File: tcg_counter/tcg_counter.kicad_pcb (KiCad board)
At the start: 2 copper layers, 63 x 88 mm, 21 parts, among them P1 TC2050-IDC-430, U1 TCAL9539RTW, U3 RF430FRL152

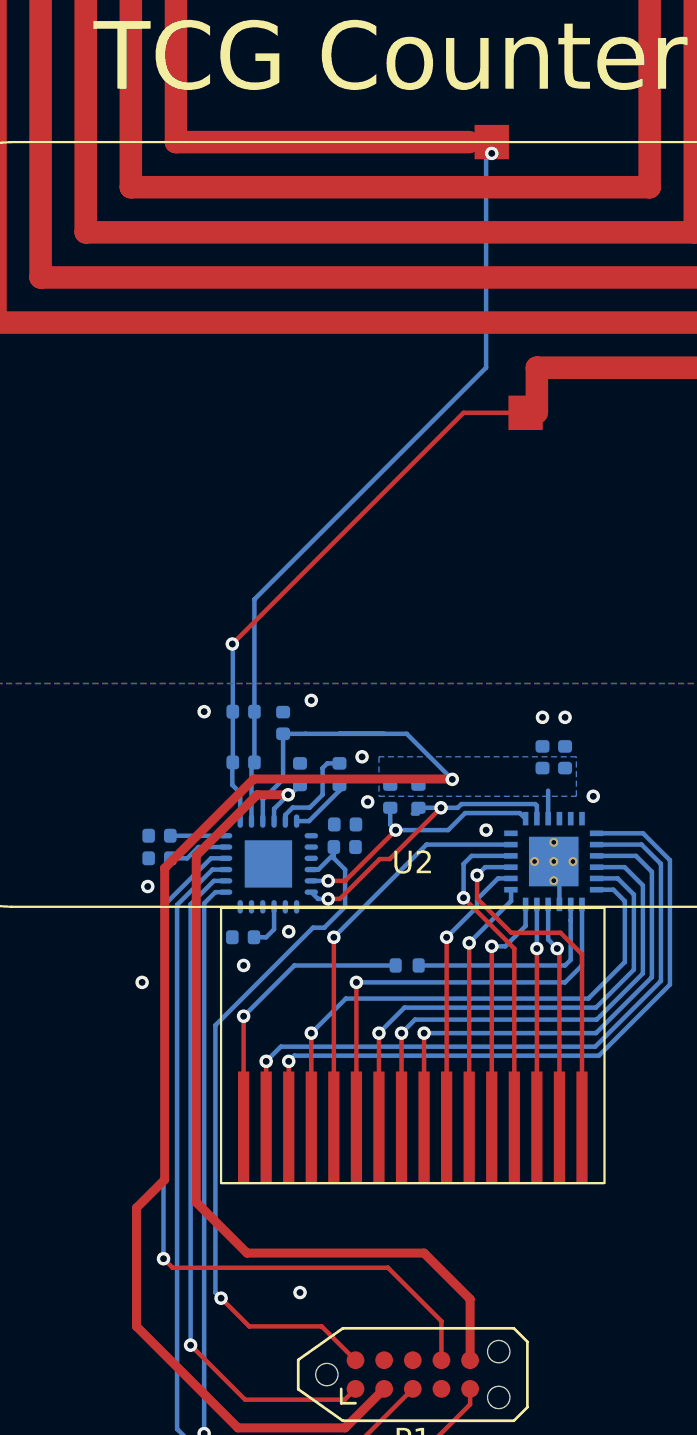
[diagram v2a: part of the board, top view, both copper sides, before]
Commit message: Cleaned up pad vias and solder paste
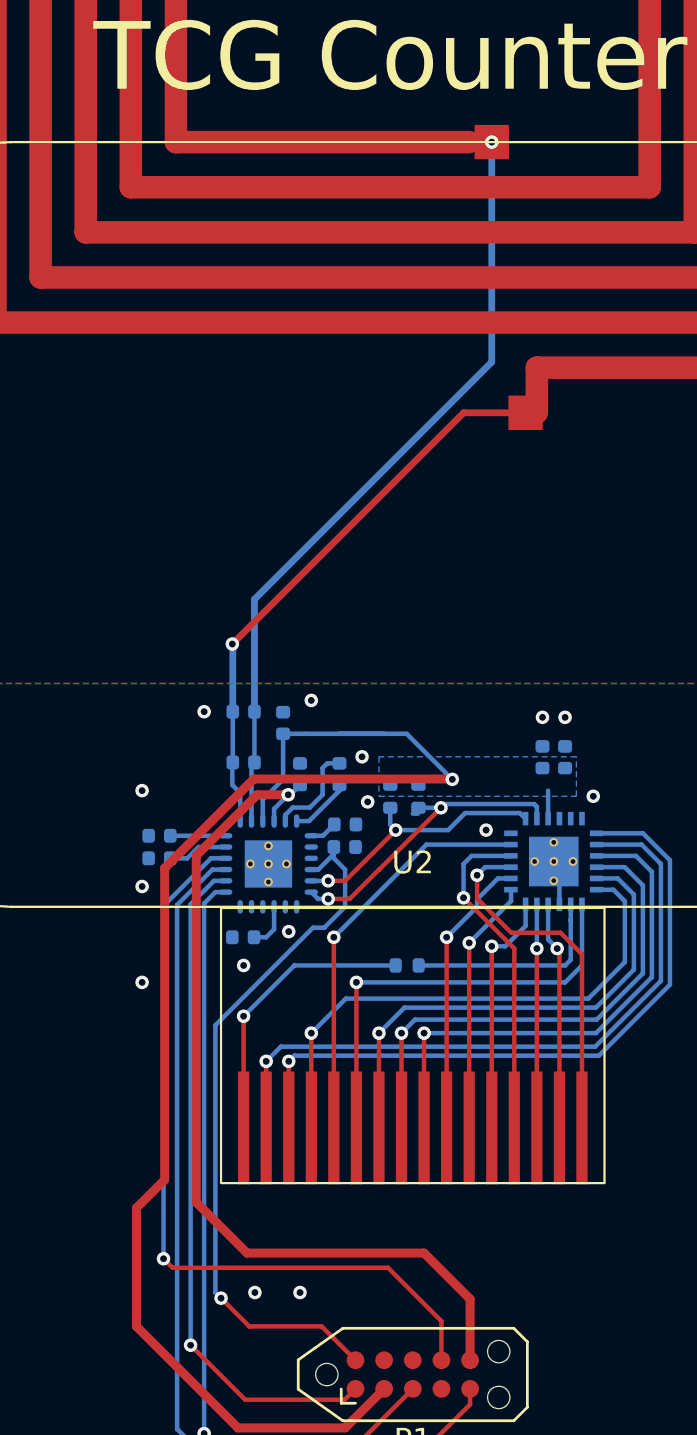
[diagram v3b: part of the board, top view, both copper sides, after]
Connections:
- U3 pad : (no net) -> GND
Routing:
- net Net-(U3-VDD2X): track 0.00 -> 1.23 mm
- net GND: track 2.00 -> 1.28 mm, vias 13 -> 15
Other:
- board text added: "U1"
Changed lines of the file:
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@@
 			(at -7.5 26.7)
 			(size 0.5 5)
-			(layers "F.Cu" "F.Paste" "F.Mask")
+			(layers "F.Cu" "F.Mask")
 			(net 18 "Net-(U2-COM)")
 			(pinfunction "COM")
@@
 			(at -6.5 26.7)
 			(size 0.5 5)
-			(layers "F.Cu" "F.Paste" "F.Mask")
+			(layers "F.Cu" "F.Mask")
 			(net 30 "Net-(U1-P01)")
 			(pinfunction "1B")
@@
 			(at -5.5 26.7)
 			(size 0.5 5)
-			(layers "F.Cu" "F.Paste" "F.Mask")
+			(layers "F.Cu" "F.Mask")
 			(net 35 "Net-(U1-P00)")
 			(pinfunction "1A")
@@
 			(at -4.5 26.7)
 			(size 0.5 5)
-			(layers "F.Cu" "F.Paste" "F.Mask")
+			(layers "F.Cu" "F.Mask")
 			(net 21 "Net-(U1-P05)")
 			(pinfunction "1F")
@@
 			(at -3.5 26.7)
 			(size 0.5 5)
-			(layers "F.Cu" "F.Paste" "F.Mask")
+			(layers "F.Cu" "F.Mask")
 			(net 37 "Net-(U1-P17)")
 			(pinfunction "3")
@@
 			(at -2.5 26.7)
 			(size 0.5 5)
-			(layers "F.Cu" "F.Paste" "F.Mask")
+			(layers "F.Cu" "F.Mask")
 			(net 22 "Net-(U1-P06)")
 			(pinfunction "1G")
@@
 			(at -1.5 26.7)
 			(size 0.5 5)
-			(layers "F.Cu" "F.Paste" "F.Mask")
+			(layers "F.Cu" "F.Mask")
 			(net 23 "Net-(U1-P04)")
 			(pinfunction "1E")
@@
 			(at -0.5 26.7)
 			(size 0.5 5)
-			(layers "F.Cu" "F.Paste" "F.Mask")
+			(layers "F.Cu" "F.Mask")
 			(net 26 "Net-(U1-P03)")
 			(pinfunction "1D")
@@
 			(at 0.5 26.7)
 			(size 0.5 5)
-			(layers "F.Cu" "F.Paste" "F.Mask")
+			(layers "F.Cu" "F.Mask")
 			(net 34 "Net-(U1-P02)")
 			(pinfunction "1C")
@@
 			(at 1.5 26.7)
 			(size 0.5 5)
-			(layers "F.Cu" "F.Paste" "F.Mask")
+			(layers "F.Cu" "F.Mask")
 			(net 29 "Net-(U1-P14)")
 			(pinfunction "2E")
@@
 			(at 2.5 26.7)
 			(size 0.5 5)
-			(layers "F.Cu" "F.Paste" "F.Mask")
+			(layers "F.Cu" "F.Mask")
 			(net 28 "Net-(U1-P13)")
 			(pinfunction "2D")
@@
 			(at 3.5 26.7)
 			(size 0.5 5)
-			(layers "F.Cu" "F.Paste" "F.Mask")
+			(layers "F.Cu" "F.Mask")
 			(net 36 "Net-(U1-P12)")
 			(pinfunction "2C")
@@
 			(at 4.5 26.7)
 			(size 0.5 5)
-			(layers "F.Cu" "F.Paste" "F.Mask")
+			(layers "F.Cu" "F.Mask")
 			(net 24 "Net-(U1-P16)")
 			(pinfunction "2G")
@@
 			(at 5.5 26.7)
 			(size 0.5 5)
-			(layers "F.Cu" "F.Paste" "F.Mask")
+			(layers "F.Cu" "F.Mask")
 			(net 27 "Net-(U1-P11)")
 			(pinfunction "2B")
@@
 			(at 6.5 26.7)
 			(size 0.5 5)
-			(layers "F.Cu" "F.Paste" "F.Mask")
+			(layers "F.Cu" "F.Mask")
 			(net 25 "Net-(U1-P10)")
 			(pinfunction "2A")
@@
 			(at 7.5 26.7)
 			(size 0.5 5)
-			(layers "F.Cu" "F.Paste" "F.Mask")
+			(layers "F.Cu" "F.Mask")
 			(net 33 "Net-(U1-P15)")
 			(pinfunction "2F")
@@
 		(at 135.100001 104 -90)
 		(property "Reference" "U3"
-			(at -3 3.600001 0)
+			(at -2.75 3.350001 180)
 			(layer "B.SilkS")
 			(effects
@@
 			(layer "Dwgs.User")
 		)
+		(pad "" thru_hole circle
+			(at -0.8 0 270)
+			(size 0.4 0.4)
+			(drill 0.2)
+			(layers "*.Cu" "B.Mask")
+			(remove_unused_layers no)
+			(net 1 "GND")
+			(zone_connect 2)
+		)
+		(pad "" thru_hole circle
+			(at 0 -0.8 270)
+			(size 0.4 0.4)
+			(drill 0.2)
+			(layers "*.Cu" "B.Mask")
+			(remove_unused_layers no)
+			(net 1 "GND")
+			(zone_connect 2)
+		)
 		(pad "" smd rect
 			(at 0 0 270)
@@
 			(layers "B.Paste")
 		)
+		(pad "" thru_hole circle
+			(at 0 0 270)
+			(size 0.4 0.4)
+			(drill 0.2)
+			(layers "*.Cu" "B.Mask")
+			(remove_unused_layers no)
+			(net 1 "GND")
+			(zone_connect 2)
+		)
+		(pad "" thru_hole circle
+			(at 0 0.8 270)
+			(size 0.4 0.4)
+			(drill 0.2)
+			(layers "*.Cu" "B.Mask")
+			(remove_unused_layers no)
+			(net 1 "GND")
+			(zone_connect 2)
+		)
+		(pad "" thru_hole circle
+			(at 0.8 0 270)
+			(size 0.4 0.4)
+			(drill 0.2)
+			(layers "*.Cu" "B.Mask")
+			(remove_unused_layers no)
+			(net 1 "GND")
+			(zone_connect 2)
+		)
 		(pad "1" smd oval
 			(at -1.899999 1.25 180)
@@
 			(size 0.4 0.4)
 			(drill 0.2)
-			(layers "*.Cu" "*.Mask")
+			(layers "*.Cu" "B.Mask")
 			(remove_unused_layers no)
 			(net 1 "GND")
@@
 			(size 0.4 0.4)
 			(drill 0.2)
-			(layers "*.Cu" "*.Mask")
+			(layers "*.Cu" "B.Mask")
 			(remove_unused_layers no)
 			(net 1 "GND")
@@
 			(size 0.4 0.4)
 			(drill 0.2)
-			(layers "*.Cu" "*.Mask")
+			(layers "*.Cu" "B.Mask")
 			(remove_unused_layers no)
 			(net 1 "GND")
@@
 			(size 0.4 0.4)
 			(drill 0.2)
-			(layers "*.Cu" "*.Mask")
+			(layers "*.Cu" "B.Mask")
 			(remove_unused_layers no)
 			(net 1 "GND")
@@
 			(size 0.4 0.4)
 			(drill 0.2)
-			(layers "*.Cu" "*.Mask")
+			(layers "*.Cu" "B.Mask")
 			(remove_unused_layers no)
 			(net 1 "GND")
@@
 			(at 0 0 270)
 			(size 2.2 2.2)
-			(layers "B.Cu" "B.Mask")
+			(layers "B.Cu" "B.Paste" "B.Mask")
 			(net 1 "GND")
 			(thermal_bridge_angle 45)
@@
 		(layer "Edge.Cuts")
 	)
+	(gr_text "U1"
+		(at 151.25 101.25 0)
+		(layer "B.SilkS")
+		(effects
+			(font
+				(size 1 1)
+				(thickness 0.15)
+			)
+			(justify mirror)
+		)
+	)
 	(gr_text "v1.0.0"
 		(at 113 130 0)
@@
 	)
 	(via
+		(at 134.5 123)
+		(size 0.6)
+		(drill 0.3)
+		(layers "F.Cu" "B.Cu")
+		(free yes)
+		(net 1)
+	)
+	(via
 		(at 148.25 97.5)
 		(size 0.6)
@@
 	)
 	(via
-		(at 129.75 105)
+		(at 129.5 105)
 		(size 0.6)
 		(drill 0.3)
@@
 		(net 1)
 	)
-	(segment
-		(start 148.000001 104.1423)
-		(end 147.750001 103.8923)
-		(width 0.2)
-		(layer "B.Cu")
-		(net 1)
-	)
-	(segment
-		(start 148.000001 104.5)
-		(end 148.000001 104.1423)
-		(width 0.2)
-		(layer "B.Cu")
+	(via
+		(at 129.5 100.75)
+		(size 0.6)
+		(drill 0.3)
+		(layers "F.Cu" "B.Cu")
+		(free yes)
 		(net 1)
 	)
@@
 	)
 	(segment
+		(start 137 102.75)
+		(end 137.52 102.75)
+		(width 0.2)
+		(layer "B.Cu")
+		(net 6)
+	)
+	(segment
+		(start 137.52 102.75)
+		(end 138.02 102.25)
+		(width 0.2)
+		(layer "B.Cu")
+		(net 6)
+	)
+	(segment
 		(start 133 123.25)
 		(end 134.25 124.5)
@@
 	)
 	(segment
-		(start 140.032843 103.782843)
-		(end 140.477157 103.782843)
+		(start 140.01 104.25)
+		(end 142.75 101.51)
 		(width 0.2)
 		(layer "F.Cu")
@@
 	)
 	(segment
-		(start 138.265683 105.550003)
-		(end 140.032843 103.782843)
+		(start 140 104.25)
+		(end 140.01 104.25)
 		(width 0.2)
 		(layer "F.Cu")
@@
 	(segment
 		(start 137.75 105.550003)
-		(end 138.265683 105.550003)
+		(end 138.699997 105.550003)
 		(width 0.2)
 		(layer "F.Cu")
@@
 	)
 	(segment
-		(start 140.477157 103.782843)
-		(end 142.75 101.51)
+		(start 138.699997 105.550003)
+		(end 140 104.25)
 		(width 0.2)
 		(layer "F.Cu")
@@
 	)
 	(segment
-		(start 146.927001 101.3444)
-		(end 143.6556 101.3444)
+		(start 146.877101 101.3444)
+		(end 142.9156 101.3444)
 		(width 0.2)
 		(layer "B.Cu")
@@
 	)
 	(segment
-		(start 137 105.25)
-		(end 137.300003 105.550003)
+		(start 147 102)
+		(end 147 101.467299)
 		(width 0.2)
 		(layer "B.Cu")
@@
 	)
 	(segment
-		(start 147 101.417399)
-		(end 146.927001 101.3444)
+		(start 137 105.25)
+		(end 137.300003 105.550003)
 		(width 0.2)
 		(layer "B.Cu")
@@
 	)
 	(segment
-		(start 143.49 101.51)
-		(end 142.75 101.51)
+		(start 147 101.467299)
+		(end 146.877101 101.3444)
 		(width 0.2)
 		(layer "B.Cu")
@@
 	)
 	(segment
-		(start 147 102)
-		(end 147 101.417399)
+		(start 142.9156 101.3444)
+		(end 142.75 101.51)
 		(width 0.2)
 		(layer "B.Cu")
@@
 	)
 	(segment
-		(start 143.6556 101.3444)
-		(end 143.49 101.51)
-		(width 0.2)
-		(layer "B.Cu")
-		(net 20)
-	)
-	(segment
 		(start 137 115.7)
 		(end 137 111.5)
@@
 		(start 143.75 84)
 		(end 146.2 84)
-		(width 0.2)
+		(width 0.3)
 		(layer "F.Cu")
 		(net 43)
@@
 		(start 133.5 94.25)
 		(end 143.75 84)
-		(width 0.2)
+		(width 0.3)
 		(layer "F.Cu")
 		(net 43)
@@
 		(start 133.52 97.25)
 		(end 133.52 94.27)
-		(width 0.2)
+		(width 0.3)
 		(layer "B.Cu")
 		(net 43)
@@
 		(net 43)
 	)
-	(segment
-		(start 145 72)
-		(end 145 72.5)
-		(width 0.2)
-		(layer "F.Cu")
-		(net 44)
-	)
 	(via
-		(at 145 72.5)
+		(at 145 72)
 		(size 0.6)
 		(drill 0.3)
@@
 	)
 	(segment
-		(start 144.75 82)
-		(end 134.48 92.27)
-		(width 0.2)
+		(start 145 72)
+		(end 145 81.75)
+		(width 0.3)
 		(layer "B.Cu")
 		(net 44)
@@
 		(start 134.48 92.27)
 		(end 134.48 97.25)
-		(width 0.2)
+		(width 0.3)
 		(layer "B.Cu")
 		(net 44)
@@
 	)
 	(segment
-		(start 144.75 72.75)
-		(end 144.75 82)
-		(width 0.2)
-		(layer "B.Cu")
-		(net 44)
-	)
-	(segment
 		(start 134.48 99.5)
 		(end 134.48 97.25)
@@
 	)
 	(segment
-		(start 145 72.5)
-		(end 144.75 72.75)
-		(width 0.2)
+		(start 145 81.75)
+		(end 134.48 92.27)
+		(width 0.3)
 		(layer "B.Cu")
 		(net 44)

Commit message: v1.0 hardware revision
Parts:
- renumbered U2 to DS1, R4 to R2, R5 to R3, U3 to U2
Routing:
- net VDDSW: track 64.4 -> 62.4 mm
